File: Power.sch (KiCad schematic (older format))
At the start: 20 parts, among them U1 MAX809S, U8 LM2596S-ADJ

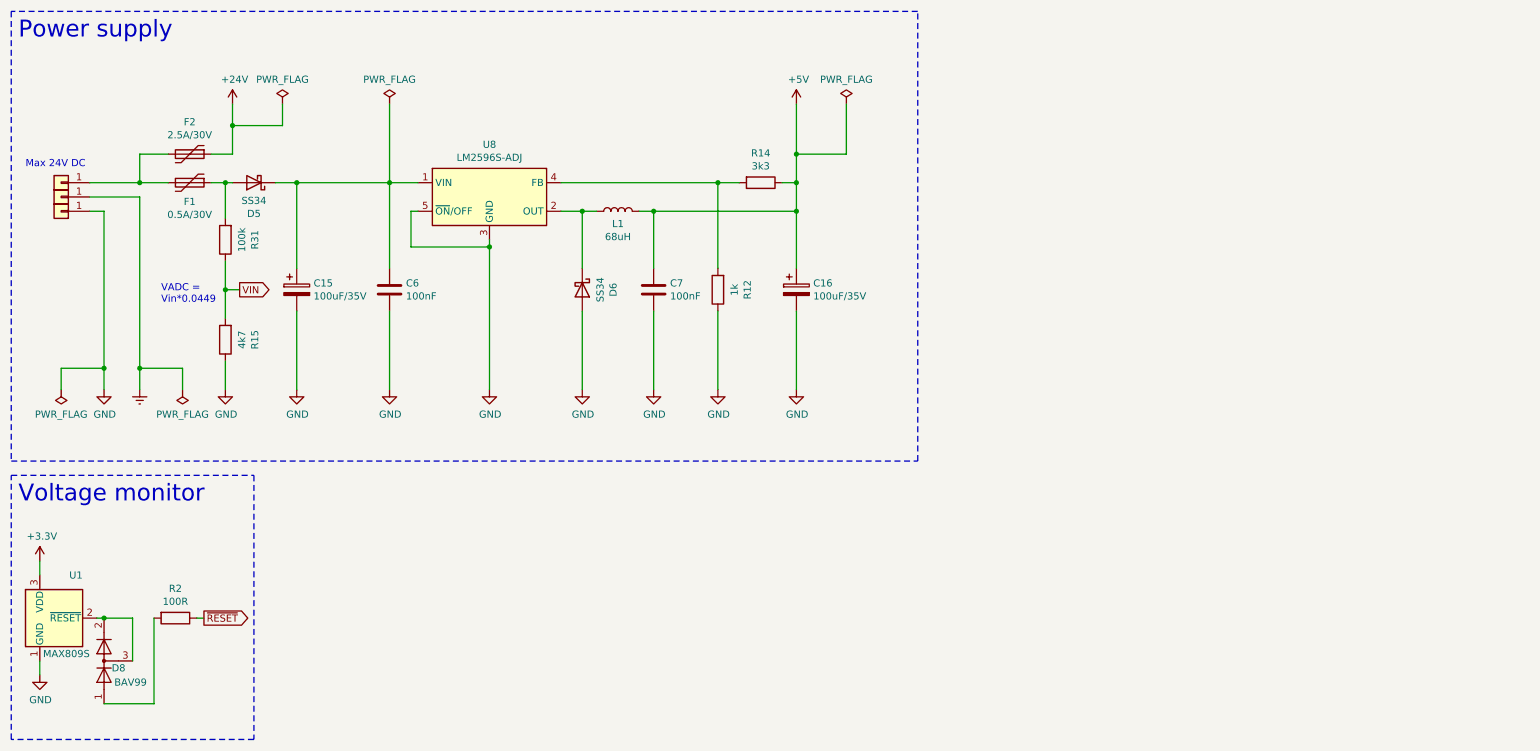
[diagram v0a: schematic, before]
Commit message: Added overheat protection that works, but very noisy.
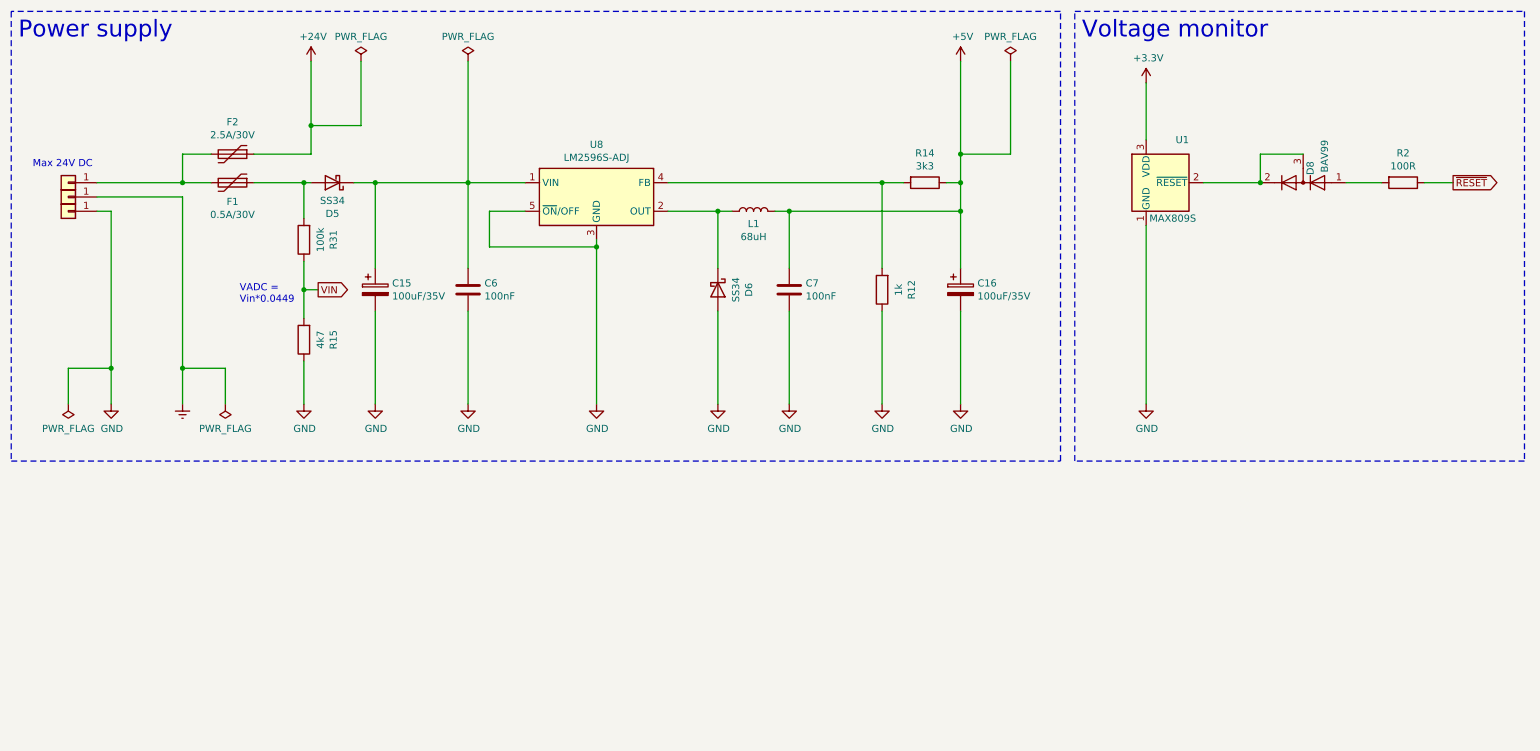
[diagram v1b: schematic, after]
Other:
- moved on the sheet: C15, C16, C6, C7, D5, D6, D8, F1, F2, L1, R12, R14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

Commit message: V2.0 pcb.
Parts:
- removed D8: BAV99, Package_TO_SOT_SMD:SOT-23, symbol Diode:BAV99
- removed R2: 100R, Resistor_SMD:R_0805_2012Metric_Pad1.20x1.40mm_HandSolder, symbol Device:R
- removed U1: MAX809S, Package_TO_SOT_SMD:SOT-23, symbol Power_Supervisor:TPS3839DBZ
- R52: renamed from R15; value 4k7 -> 4k7 1%
- R70: renamed from R31; value 100k -> 100k 1%
- renumbered C6 to C33, C7 to C34, C15 to C70, C16 to C71, D5 to D6, D6 to D7, F2 to F1, F1 to F2, J101 to J6, J102 to J7, J103 to J8, R12 to R31, R14 to R40, U8 to U5
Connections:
- net 24V_DC_SW: now reaches C33.1, C70.1, D6.1 (K), U5.1 (VIN)
- net 24V_DC: now reaches F1.2, F2.2, J6.1 (Pin_1)
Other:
- note removed: "Voltage monitor"

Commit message: V2.0 pcb.
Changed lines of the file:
@@
 Sheet 3 5
 Title "IoT12-hardware power supply"
-Date "2021-02-21"
+Date "2021-02-22"
 Rev "V2.0"
 Comp ""
@@
 	1    0    0    -1
 $EndComp
-Wire Wire Line
-	1250 1950 1250 3050
-$Comp
-L power:PWR_FLAG #FLG0106
-U 1 1 6072A30C
-P 900 3300
-F 0 "#FLG0106" H 900 3375 50  0001 C CNN
-F 1 "PWR_FLAG" H 900 3473 50  0000 C CNN
-F 2 "" H 900 3300 50  0001 C CNN
-F 3 "~" H 900 3300 50  0001 C CNN
-	1    900  3300
-	-1   0    0    1
-$EndComp
-Wire Wire Line
-	1250 3050 900  3050
-Wire Wire Line
-	900  3050 900  3300
-Connection ~ 1250 3050
-Wire Wire Line
-	1250 3050 1250 3300
 Text Label 1300 1750 0    50   ~ 0
 24V_DC
 Text Label 3200 1750 0    50   ~ 0
 24V_DC_SW
+Wire Wire Line
+	1250 1950 1250 3300
 $EndSCHEMATC
